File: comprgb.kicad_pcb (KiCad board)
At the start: 2 copper layers, 50 x 70 mm, 42 parts, among them J1 VGA, J2 Conn_01x03_Male, J3 USB_C_Receptacle_Power, J4 SCART_CONN, J5 3xRCA_CONN, U1 MCP1700-2802E_SOT23, U2 LMH1251MT_NOPB, U3 TPF144-VR, U6 74AHC1G86, U7 74AHC1G86

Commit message: bigger gote
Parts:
- added R12: 200, Resistor_SMD:R_0805_2012Metric, F.Cu at (38.0, 60.0)
- added R13: 200, Resistor_SMD:R_0805_2012Metric, F.Cu at (38.0, 64.4)
- FID2: footprint videobits:uwusmaller -> videobits:uwuriel
- moved FID2 7.11 mm to (53.9, 97.5)
- moved C8 0.30 mm to (39.5, 44.4)
- moved FB1 0.30 mm to (33.0, 43.3)
- moved U1 0.30 mm to (42.7, 44.4)
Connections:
- J1 pad 13: /HSYNC -> /CSYNC
- J4 pad 19: /HSYNC -> Net-(J4-Pad19)
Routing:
- net /HSYNC: track 30.2 -> 0.00 mm
- net /CSYNC: track 0.00 -> 28.0 mm
- net VCC: track 139.5 -> 132.5 mm
- net Net-(J4-Pad19): track 0.00 -> 3.64 mm
- net Net-(R12-Pad2): track 0.00 -> 2.59 mm
- net GND: track 26.3 -> 23.8 mm, vias 88 -> 90
- net Net-(U2-Pad14): track 25.7 -> 27.4 mm
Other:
- board text added: "YPbPr to RGB 2021-09-23 rev 1.2 wakabavideo.com"
- board text removed: "YPbPr 2 RGB 2019-10-27 rev 1.1 wakabavideo.com"

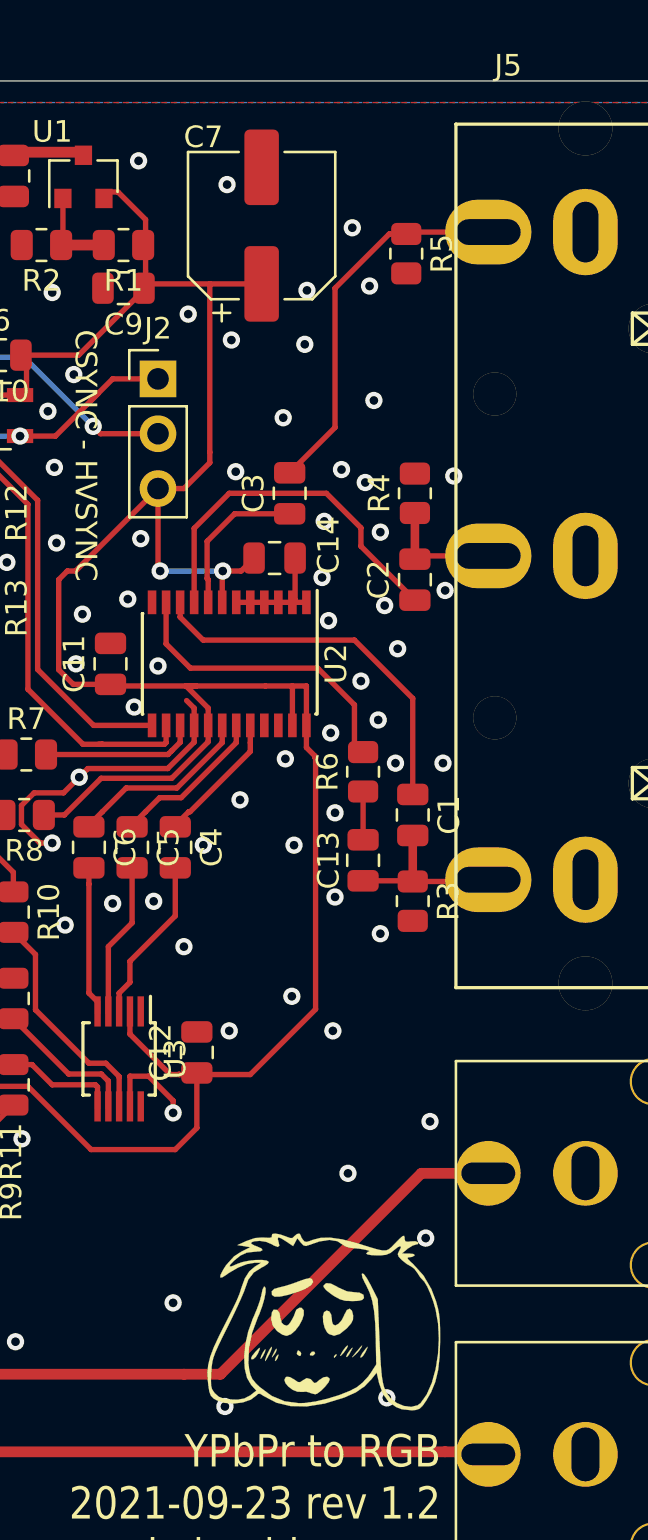
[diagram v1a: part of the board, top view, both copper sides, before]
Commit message: add power led, rebuild gerb
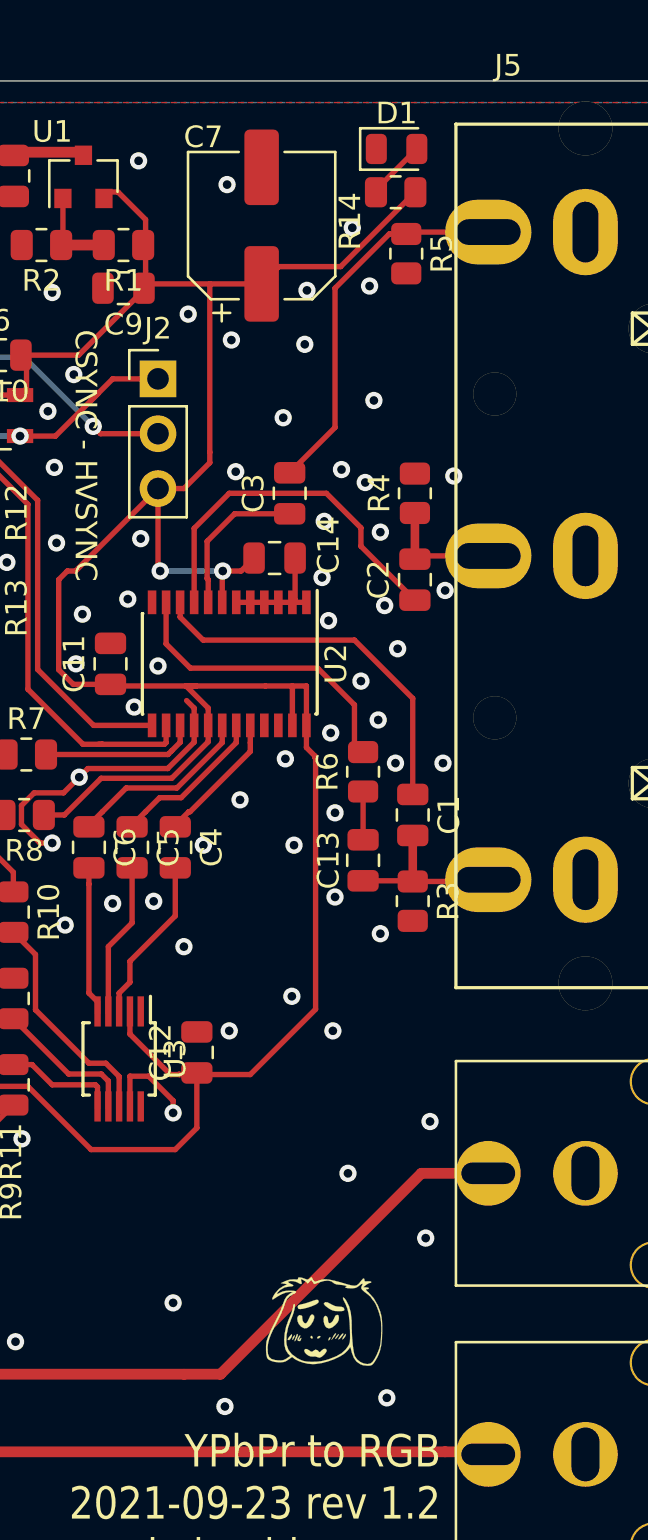
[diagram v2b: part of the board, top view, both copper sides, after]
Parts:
- added D1: LED, LED_SMD:LED_0805_2012Metric, F.Cu at (57.2, 43.1)
- added R14: 1k5, Resistor_SMD:R_0805_2012Metric, F.Cu at (57.2, 45.2)
- FID2: footprint videobits:uwuriel -> videobits:uwusmaller
- R2: value 1k33 -> 1k5
- U1: value MCP1700-2802E_SOT23 -> AP2125N-1.8TRG1
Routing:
- net VCC: track 132.5 -> 141.4 mm
- net Net-(D1-Pad2): track 0.00 -> 2.79 mm

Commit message: updated version no
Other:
- board text added: "YPbPr to RGB 2021-11-28 rev 1.3 wakabavideo.com"
- board text removed: "YPbPr to RGB 2021-09-23 rev 1.2 wakabavideo.com"

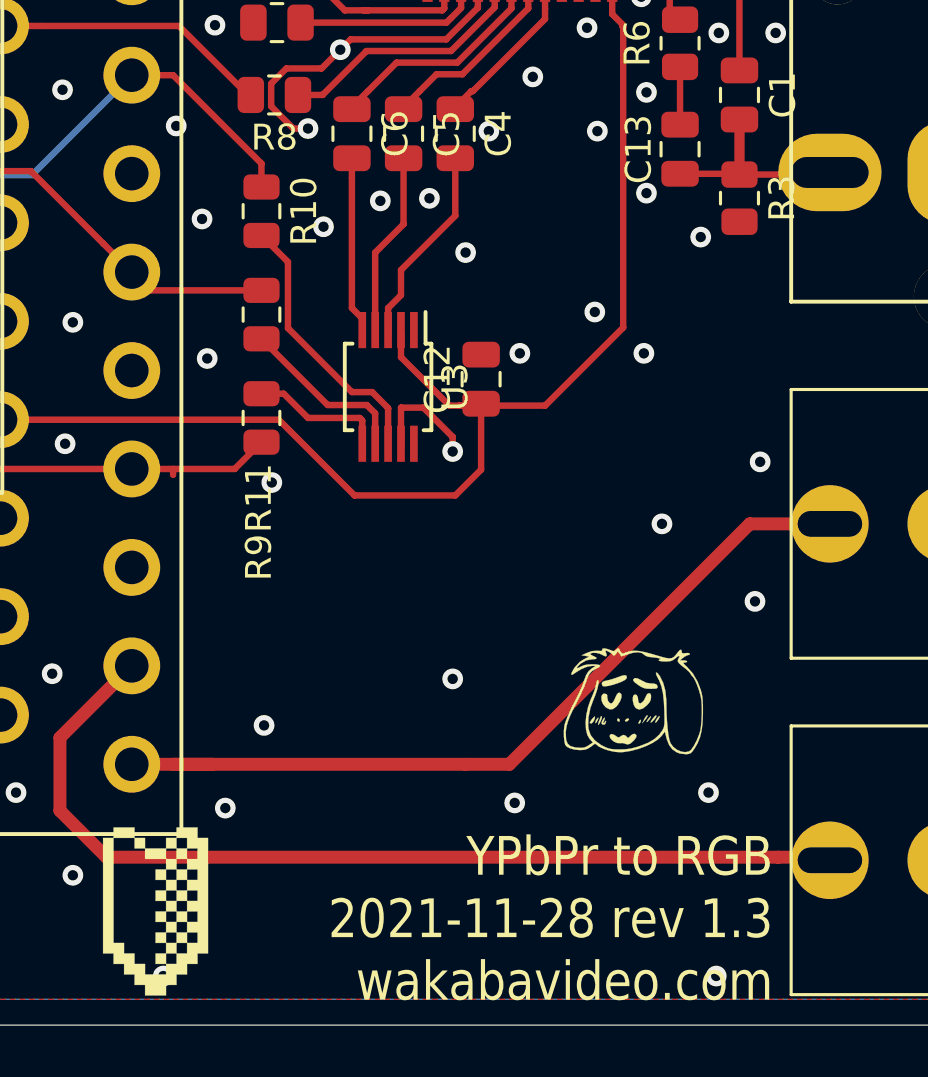
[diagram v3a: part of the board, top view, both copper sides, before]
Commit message: swap video amp to THS7374 for parts availability
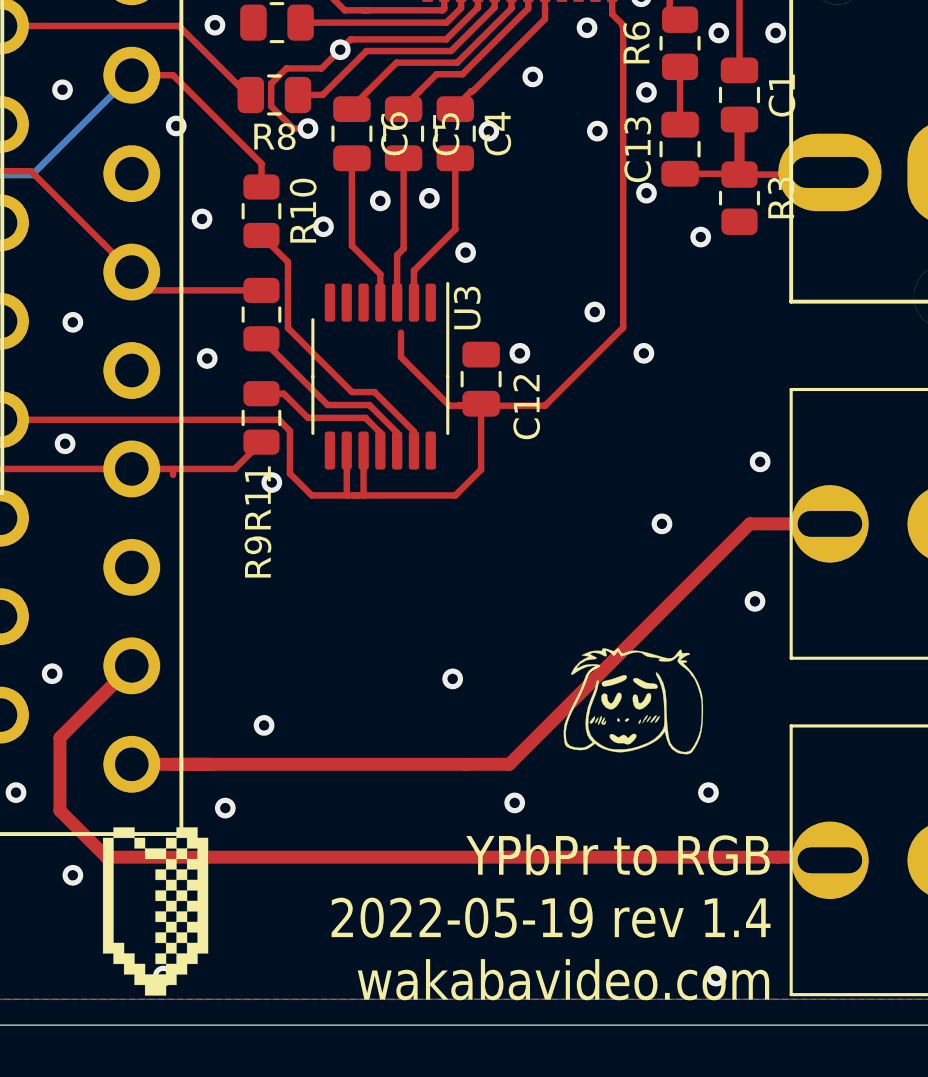
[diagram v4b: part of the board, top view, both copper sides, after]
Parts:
- U1: value AP2125N-1.8TRG1 -> RT9166-18GVL(Z00)
- U3: value TPF144-VR -> THS7374; footprint Package_SO:MSOP-10_3x3mm_P0.5mm -> Package_SO:TSSOP-14_4.4x5mm_P0.65mm
- moved U3 0.50 mm to (44.1, 84.9)
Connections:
- net /SYNC renamed Net-(U3-Pad1)
- U3 pad 10: Net-(U3-Pad10) -> VCC
- U3 pad 2: VCC -> Net-(C4-Pad2)
- U3 pad 3: Net-(C4-Pad2) -> Net-(C5-Pad2)
- U3 pad 4: Net-(C5-Pad2) -> Net-(C6-Pad2)
- U3 pad 5: Net-(C6-Pad2) -> GND
- U3 pad 6: Net-(R9-Pad2) -> GND
- U3 pad 7: Net-(R11-Pad2) -> Net-(U3-Pad7)
- U3 pad 8: Net-(R10-Pad2) -> Net-(U3-Pad8)
- U3 pad 9: GND -> VCC
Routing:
- net VCC: track 141.4 -> 146.0 mm
- net GND: track 23.8 -> 19.3 mm, vias 90 -> 89
- net Net-(C4-Pad2): track 7.75 -> 6.25 mm
- net Net-(C5-Pad2): track 7.13 -> 5.69 mm
- net Net-(R10-Pad2): track 10.2 -> 11.3 mm
- net Net-(C6-Pad2): track 6.84 -> 5.97 mm
- net Net-(R9-Pad2): track 5.33 -> 5.91 mm
- net Net-(R11-Pad2): track 6.87 -> 7.44 mm
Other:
- board text added: "YPbPr to RGB 2022-05-19 rev 1.4 wakabavideo.com"
- board text removed: "YPbPr to RGB 2021-11-28 rev 1.3 wakabavideo.com"

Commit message: update to kicad 8, production files
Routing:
- net GND: track 19.3 -> 18.0 mm
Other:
- net class Default removed

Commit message: new prod files
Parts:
- FID2: footprint videobits:uwusmaller -> videobits:uwuriel
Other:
- board text added: "YPbPr to RGB 2025-09-13 rev 1.6 wakabavideo.com"
- board text removed: "YPbPr to RGB 2022-05-19 rev 1.4 wakabavideo.com"
